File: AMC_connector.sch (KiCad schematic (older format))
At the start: 2 parts, among them P3 CMP-0001-00058-2

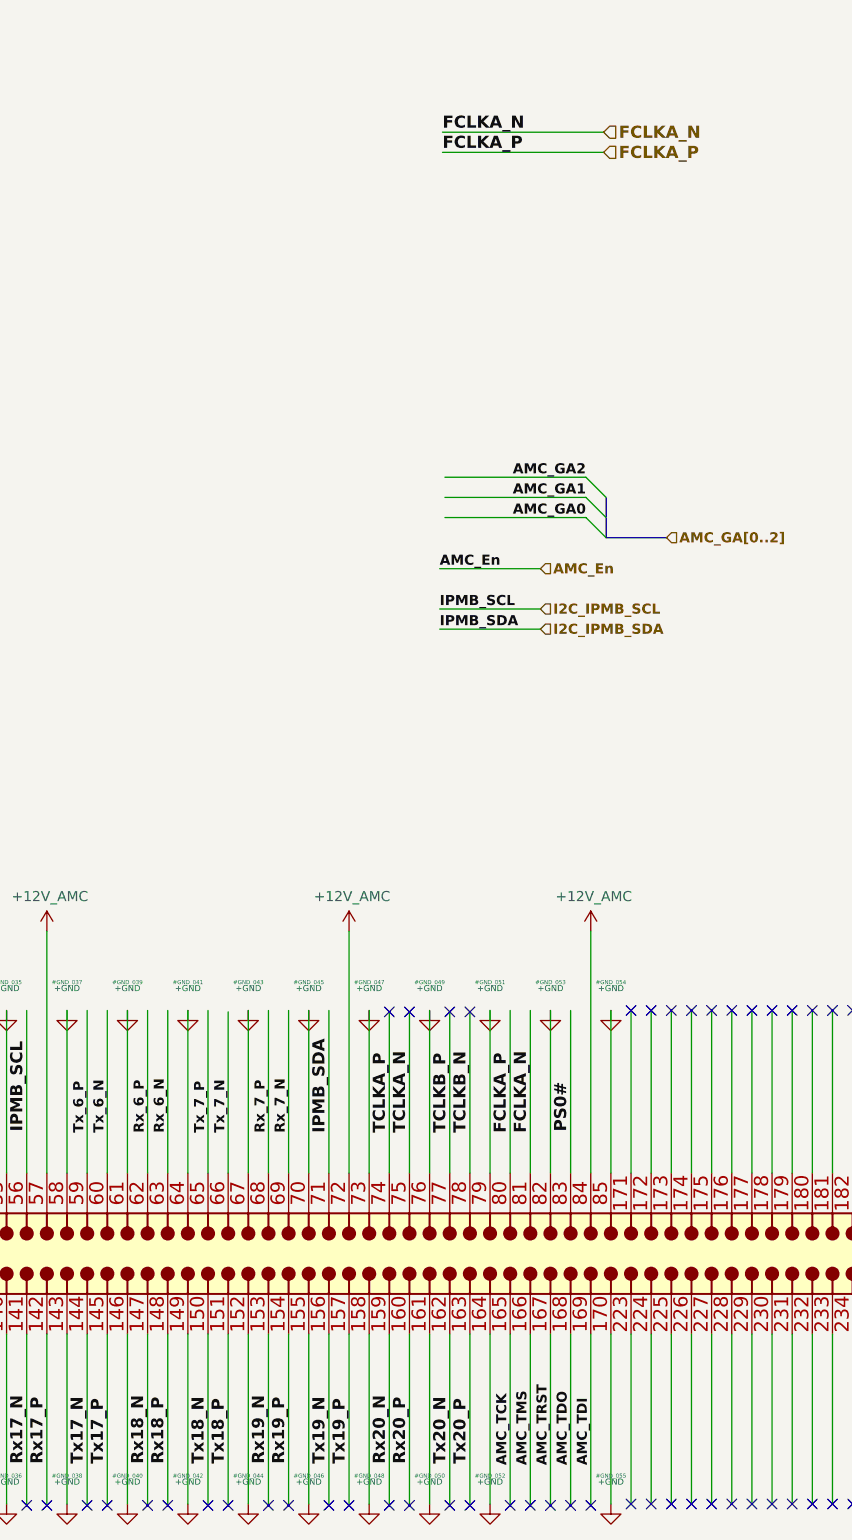
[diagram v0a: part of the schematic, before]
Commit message: less traces under SFP cage, MLVDS transceiver added, TCLKA connected to FPGA
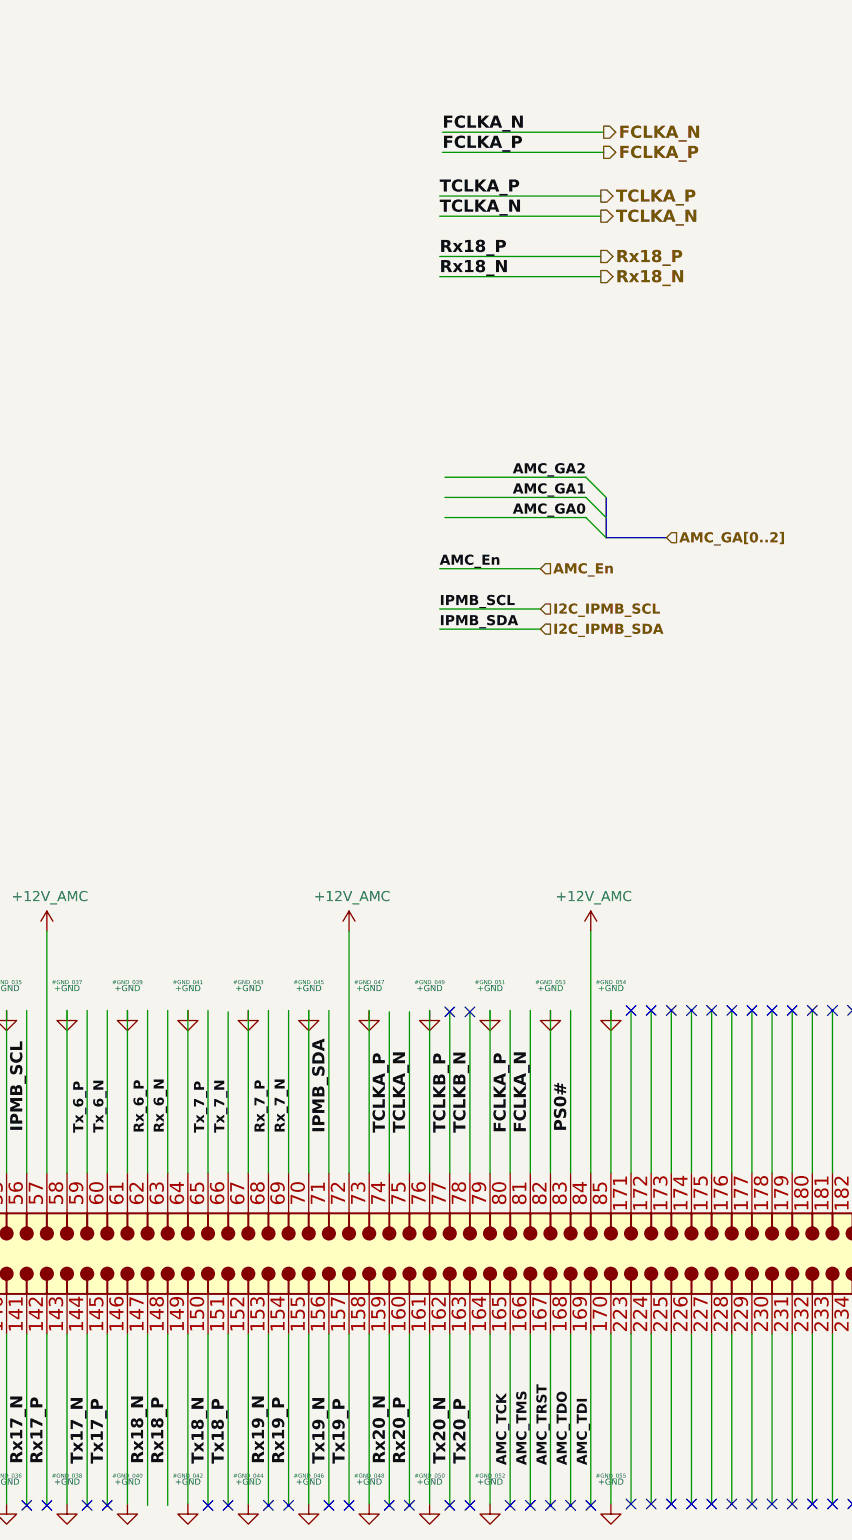
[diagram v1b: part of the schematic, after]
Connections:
- wire segments 310 -> 314
- no-connect marks 179 -> 175
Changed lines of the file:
@@
 Text Label 9214 2633 0    60   ~ 12
 FCLKA_P
-Text HLabel 10014 2533 2    60   Input ~ 12
+Text HLabel 10014 2533 2    60   Output ~ 12
 FCLKA_N
-Text HLabel 10014 2633 2    60   Input ~ 12
+Text HLabel 10014 2633 2    60   Output ~ 12
 FCLKA_P
 Text Label 6250 7500 1    50   ~ 10
@@
 NoConn ~ 8150 9350
 NoConn ~ 8050 9350
-NoConn ~ 7850 9350
-NoConn ~ 7750 9350
 NoConn ~ 7550 9350
 NoConn ~ 7450 9350
@@
 NoConn ~ 5350 6900
 NoConn ~ 5450 6900
-NoConn ~ 8950 6900
-NoConn ~ 9050 6900
 NoConn ~ 9250 6900
 NoConn ~ 9350 6900
+Text Label 9200 2850 0    60   ~ 12
+TCLKA_P
+Text Label 9200 2950 0    60   ~ 12
+TCLKA_N
+Wire Wire Line
+	10000 2850 9200 2850
+Wire Wire Line
+	10000 2950 9200 2950
+Text HLabel 10000 2850 2    60   Output ~ 12
+TCLKA_P
+Text HLabel 10000 2950 2    60   Output ~ 12
+TCLKA_N
+Text Label 9200 3250 0    60   ~ 12
+Rx18_N
+Text Label 9200 3150 0    60   ~ 12
+Rx18_P
+Text HLabel 10000 3150 2    60   Output ~ 12
+Rx18_P
+Text HLabel 10000 3250 2    60   Output ~ 12
+Rx18_N
+Wire Wire Line
+	9200 3150 10000 3150
+Wire Wire Line
+	9200 3250 10000 3250
 Wire Bus Line
 	10026 4346 10026 4546

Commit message: BOM configuration file edited, updated Marble picture, some components part number changed
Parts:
- D1: symbol Diodes:SS16 -> AMC_FMC_Carrier-PcbDoc-rescue:SS16-Diodes
- P3: config (none) -> dnf
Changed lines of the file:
@@
 F 2 "moja:AMC-GF-2D-750-O274" H 1550 7900 60  0001 C CNN
 F 3 "" H 1550 7900 60  0000 C CNN
+F 4 "dnf" H 1550 7900 50  0001 C CNN "config"
 	1    1550 7900
 	1    0    0    -1
@@
 	3350 7700 3350 6500
 $Comp
-L Diodes:SS16 D1
+L AMC_FMC_Carrier-PcbDoc-rescue:SS16-Diodes D1
 U 1 1 5CAB1052
 P 12000 5400

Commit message: Rename library AMC_FMC_Carrier-PcbDoc-rescue as marble_misc
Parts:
- D1: symbol AMC_FMC_Carrier-PcbDoc-rescue:SS16-Diodes -> marble_misc:SS16-Diodes
- P3: symbol AMC_FMC_Carrier-PcbDoc-rescue:CMP-0001-00058-2-AMC-AMC_FMC_Carrier-PcbDoc-rescue -> marble_misc:CMP-0001-00058-2-AMC-AMC_FMC_Carrier-PcbDoc-rescue
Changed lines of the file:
@@
 $EndDescr
 $Comp
-L AMC_FMC_Carrier-PcbDoc-rescue:CMP-0001-00058-2-AMC-AMC_FMC_Carrier-PcbDoc-rescue P?
+L marble_misc:CMP-0001-00058-2-AMC-AMC_FMC_Carrier-PcbDoc-rescue P?
 U 1 1 5BD3210B
 P 1550 7900
@@
 Tx_7_P
 $Comp
-L AMC_FMC_Carrier-PcbDoc-rescue:+12V_AMC-powerMG-AMC_FMC_Carrier-PcbDoc-rescue #PWR029
+L marble_misc:+12V_AMC-powerMG-AMC_FMC_Carrier-PcbDoc-rescue #PWR029
 U 1 1 5DEC6F0B
 P 1750 6500
@@
 	1750 6500 1750 7700
 $Comp
-L AMC_FMC_Carrier-PcbDoc-rescue:+12V_AMC-powerMG-AMC_FMC_Carrier-PcbDoc-rescue #PWR031
+L marble_misc:+12V_AMC-powerMG-AMC_FMC_Carrier-PcbDoc-rescue #PWR031
 U 1 1 5DF1FECB
 P 2450 6500
@@
 $EndComp
 $Comp
-L AMC_FMC_Carrier-PcbDoc-rescue:+12V_AMC-powerMG-AMC_FMC_Carrier-PcbDoc-rescue #PWR032
+L marble_misc:+12V_AMC-powerMG-AMC_FMC_Carrier-PcbDoc-rescue #PWR032
 U 1 1 5DF4CACF
 P 3350 6500
@@
 $EndComp
 $Comp
-L AMC_FMC_Carrier-PcbDoc-rescue:+12V_AMC-powerMG-AMC_FMC_Carrier-PcbDoc-rescue #PWR033
+L marble_misc:+12V_AMC-powerMG-AMC_FMC_Carrier-PcbDoc-rescue #PWR033
 U 1 1 5DFD25BA
 P 4250 6500
@@
 $EndComp
 $Comp
-L AMC_FMC_Carrier-PcbDoc-rescue:+12V_AMC-powerMG-AMC_FMC_Carrier-PcbDoc-rescue #PWR034
+L marble_misc:+12V_AMC-powerMG-AMC_FMC_Carrier-PcbDoc-rescue #PWR034
 U 1 1 5DFFEFC3
 P 5750 6500
@@
 $EndComp
 $Comp
-L AMC_FMC_Carrier-PcbDoc-rescue:+12V_AMC-powerMG-AMC_FMC_Carrier-PcbDoc-rescue #PWR035
+L marble_misc:+12V_AMC-powerMG-AMC_FMC_Carrier-PcbDoc-rescue #PWR035
 U 1 1 5E02B9CC
 P 7250 6500
@@
 $EndComp
 $Comp
-L AMC_FMC_Carrier-PcbDoc-rescue:+12V_AMC-powerMG-AMC_FMC_Carrier-PcbDoc-rescue #PWR036
+L marble_misc:+12V_AMC-powerMG-AMC_FMC_Carrier-PcbDoc-rescue #PWR036
 U 1 1 5E0583D5
 P 8750 6500
@@
 $EndComp
 $Comp
-L AMC_FMC_Carrier-PcbDoc-rescue:+12V_AMC-powerMG-AMC_FMC_Carrier-PcbDoc-rescue #PWR037
+L marble_misc:+12V_AMC-powerMG-AMC_FMC_Carrier-PcbDoc-rescue #PWR037
 U 1 1 5E084DDE
 P 9950 6500
@@
 	3350 7700 3350 6500
 $Comp
-L AMC_FMC_Carrier-PcbDoc-rescue:SS16-Diodes D1
+L marble_misc:SS16-Diodes D1
 U 1 1 5CAB1052
 P 12000 5400

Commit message: Strip extraneous AMC_FMC_Carrier-PcbDoc-rescue and powerMG from symbol names
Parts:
- P3: symbol marble_misc:CMP-0001-00058-2-AMC-AMC_FMC_Carrier-PcbDoc-rescue -> marble_misc:CMP-0001-00058-2-AMC
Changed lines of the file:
@@
 $EndDescr
 $Comp
-L marble_misc:CMP-0001-00058-2-AMC-AMC_FMC_Carrier-PcbDoc-rescue P?
+L marble_misc:CMP-0001-00058-2-AMC P?
 U 1 1 5BD3210B
 P 1550 7900
@@
 Tx_7_P
 $Comp
-L marble_misc:+12V_AMC-powerMG-AMC_FMC_Carrier-PcbDoc-rescue #PWR029
+L marble_misc:+12V_AMC #PWR029
 U 1 1 5DEC6F0B
 P 1750 6500
@@
 	1750 6500 1750 7700
 $Comp
-L marble_misc:+12V_AMC-powerMG-AMC_FMC_Carrier-PcbDoc-rescue #PWR031
+L marble_misc:+12V_AMC #PWR031
 U 1 1 5DF1FECB
 P 2450 6500
@@
 $EndComp
 $Comp
-L marble_misc:+12V_AMC-powerMG-AMC_FMC_Carrier-PcbDoc-rescue #PWR032
+L marble_misc:+12V_AMC #PWR032
 U 1 1 5DF4CACF
 P 3350 6500
@@
 $EndComp
 $Comp
-L marble_misc:+12V_AMC-powerMG-AMC_FMC_Carrier-PcbDoc-rescue #PWR033
+L marble_misc:+12V_AMC #PWR033
 U 1 1 5DFD25BA
 P 4250 6500
@@
 $EndComp
 $Comp
-L marble_misc:+12V_AMC-powerMG-AMC_FMC_Carrier-PcbDoc-rescue #PWR034
+L marble_misc:+12V_AMC #PWR034
 U 1 1 5DFFEFC3
 P 5750 6500
@@
 $EndComp
 $Comp
-L marble_misc:+12V_AMC-powerMG-AMC_FMC_Carrier-PcbDoc-rescue #PWR035
+L marble_misc:+12V_AMC #PWR035
 U 1 1 5E02B9CC
 P 7250 6500
@@
 $EndComp
 $Comp
-L marble_misc:+12V_AMC-powerMG-AMC_FMC_Carrier-PcbDoc-rescue #PWR036
+L marble_misc:+12V_AMC #PWR036
 U 1 1 5E0583D5
 P 8750 6500
@@
 $EndComp
 $Comp
-L marble_misc:+12V_AMC-powerMG-AMC_FMC_Carrier-PcbDoc-rescue #PWR037
+L marble_misc:+12V_AMC #PWR037
 U 1 1 5E084DDE
 P 9950 6500

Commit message: Symbols lib. and schematic: update footprint fields
sync with layout is now possible without errors
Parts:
- P3: footprint moja:AMC-GF-2D-750-O274 -> Marble:AMC-GF-2D-750-O274
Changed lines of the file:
@@
 F 0 "P3" H 1520 7753 60  0000 R CNN
 F 1 "CMP-0001-00058-2" H 1520 7647 60  0000 R CNN
-F 2 "moja:AMC-GF-2D-750-O274" H 1550 7900 60  0001 C CNN
+F 2 "Marble:AMC-GF-2D-750-O274" H 1550 7900 60  0001 C CNN
 F 3 "" H 1550 7900 60  0000 C CNN
 F 4 "dnf" H 1550 7900 50  0001 C CNN "config"

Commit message: SCH: rename +3.3VP, 3V3PM and +3V3MP to +3V3P
  * all of them refer to the same net
  * to make confusion perfect, all 3 power symbols on the schematic
    were an instance of the symbol `+3.3VP` with different
    value attributes
  * renamed the `+3.3VP` symbol to `+3V3P` for naming consistency
  * SCH: replaced all power symbols on the net by the new one
  * PCB: still needs to be synced up, as the net name has changed
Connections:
- net labels added: +3V3P
- net labels removed: 3V3PM
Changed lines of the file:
@@
 	3800 4450 4150 4450
 $Comp
-L power:+3.3VP #PWR0631
+L power:+3V3P #PWR0631
 U 1 1 5D7C0506
 P 1950 6700
+AR Path="/5D7C0506" Ref="#PWR0631"  Part="1"
+AR Path="/5BD320D5/5D7C0506" Ref="#PWR0631"  Part="1"
 F 0 "#PWR0631" H 1955 6840 50  0001 C CNN
-F 1 "3V3PM" H 1935 6873 50  0000 C CNN
+F 1 "+3V3P" H 1935 6873 50  0000 C CNN
 F 2 "" H 1950 6700 50  0001 C CNN
 F 3 "" H 1950 6700 50  0001 C CNN
